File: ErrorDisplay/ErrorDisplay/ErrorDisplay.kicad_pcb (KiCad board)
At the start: 2 copper layers, 195 x 55 mm, 0 parts

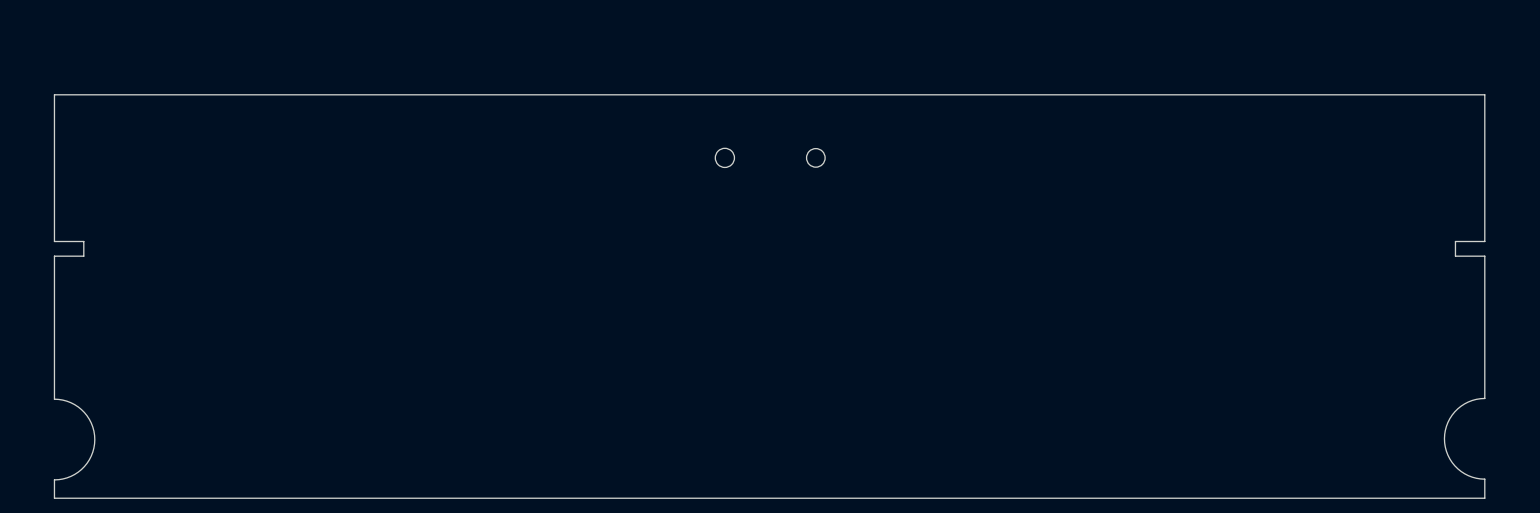
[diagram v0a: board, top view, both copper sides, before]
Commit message: Close Placement of Motors. Need Mechanical Fit check first
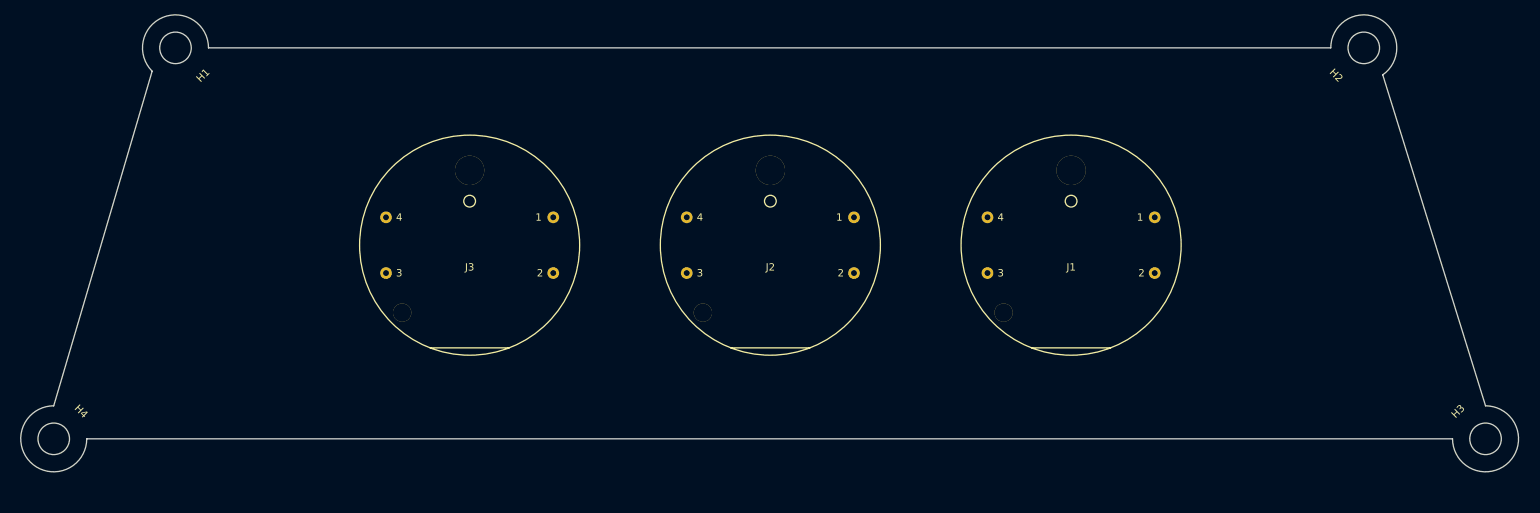
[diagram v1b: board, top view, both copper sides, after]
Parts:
- added H1: MountingHole, MountingHole:MountingHole_4.3mm_M4, F.Cu at (64.0, 82.4)
- added H2: MountingHole, MountingHole:MountingHole_4.3mm_M4, F.Cu at (226.0, 82.4)
- added H3: MountingHole, MountingHole:MountingHole_4.3mm_M4, F.Cu at (242.6, 135.7)
- added H4: MountingHole, MountingHole:MountingHole_4.3mm_M4, F.Cu at (47.4, 135.7)
- added J1: X27Motor, Library:X27-168, F.Cu at (186.1, 109.3)
- added J2: X27Motor, Library:X27-168, F.Cu at (145.1, 109.3)
- added J3: X27Motor, Library:X27-168, F.Cu at (104.1, 109.3)
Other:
- board size 195 x 55 mm -> 204.2 x 62.3 mm
- board text added: "Motor Spindle 18.5mm"

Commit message: WIP - Test build for the Stepper Driver
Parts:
- added J4: Conn_01x04_Pin, Library:CONN_70551-xxxx_04_MOL, B.Cu at (221.2, 110.9)
- H1, H2, H3, H4: footprint MountingHole:MountingHole_4.3mm_M4 -> MountingHole:MountingHole_5.3mm_M5
- moved H1 3.20 mm to (66.5, 84.4)
- moved H2 3.20 mm to (223.5, 84.4)
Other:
- board size 204.2 x 62.3 mm -> 205.9 x 62 mm

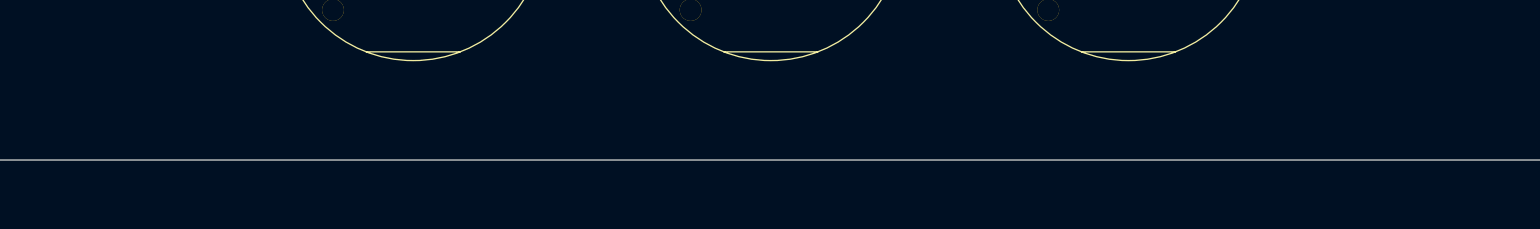
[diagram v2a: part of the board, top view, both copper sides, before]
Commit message: LEDs outlined. Colors Chosen.
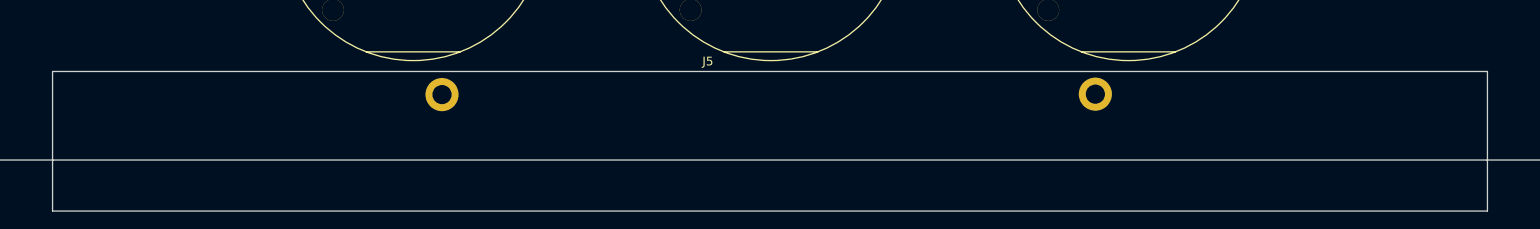
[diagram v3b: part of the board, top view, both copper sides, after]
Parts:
- added J5: Conn_01x01_Pin, Library:DigitalSegment, F.Cu at (137.9, 125.7)
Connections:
- net /Motors/P0_0 renamed /MCU/P0_0
- net /Motors/P0_1 renamed /MCU/P0_1
- net /Motors/P0_2 renamed /MCU/P0_2
- net /Motors/P0_3 renamed /MCU/P0_3
- net /Motors/P1_0 renamed /MCU/P1_0
- net /Motors/P1_1 renamed /MCU/P1_1
- net /Motors/P1_2 renamed /MCU/P1_2
- net /Motors/P1_3 renamed /MCU/P1_3
- net /Motors/P2_0 renamed /MCU/P2_0
- net /Motors/P2_1 renamed /MCU/P2_1
- net /Motors/P2_2 renamed /MCU/P2_2
- net /Motors/P2_3 renamed /MCU/P2_3
